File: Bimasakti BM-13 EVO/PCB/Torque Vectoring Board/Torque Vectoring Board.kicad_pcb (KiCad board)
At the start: 2 copper layers, 63.6 x 82.8 mm, 1 part

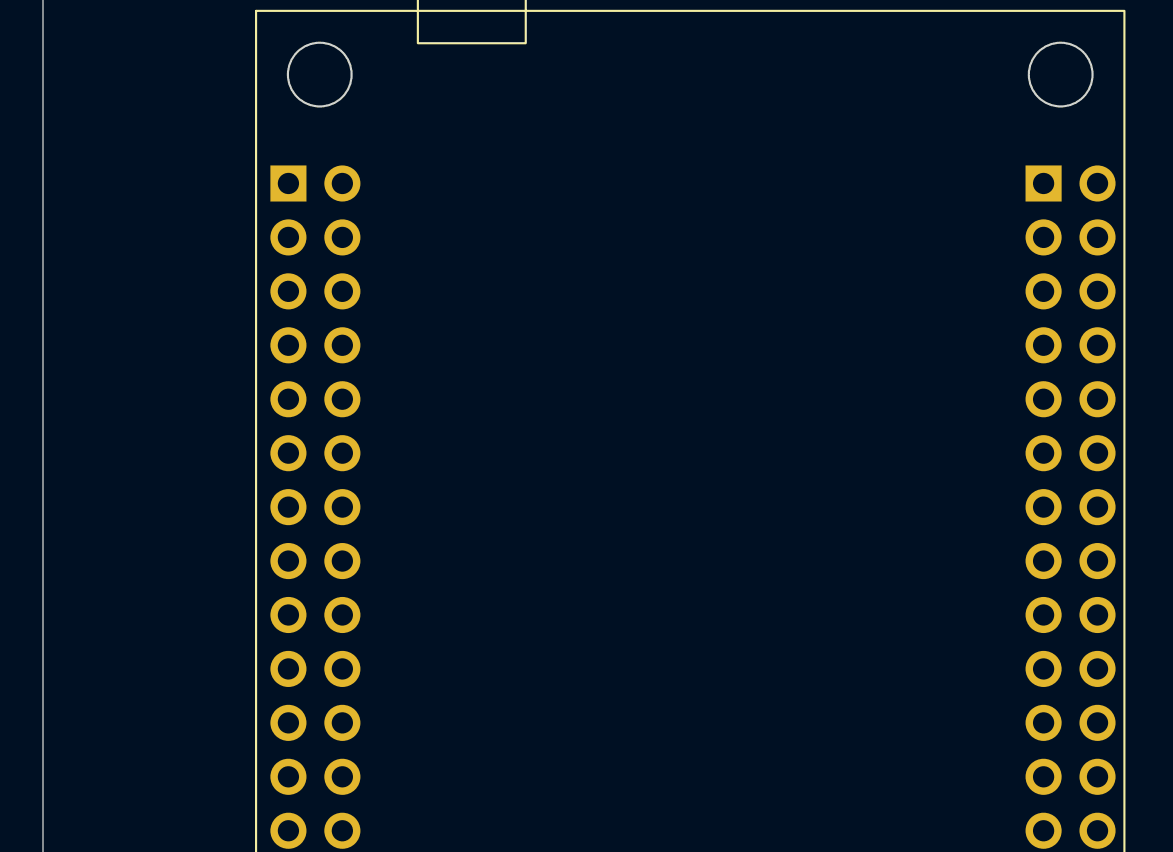
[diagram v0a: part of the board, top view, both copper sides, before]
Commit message: pdm finishing tambah logo
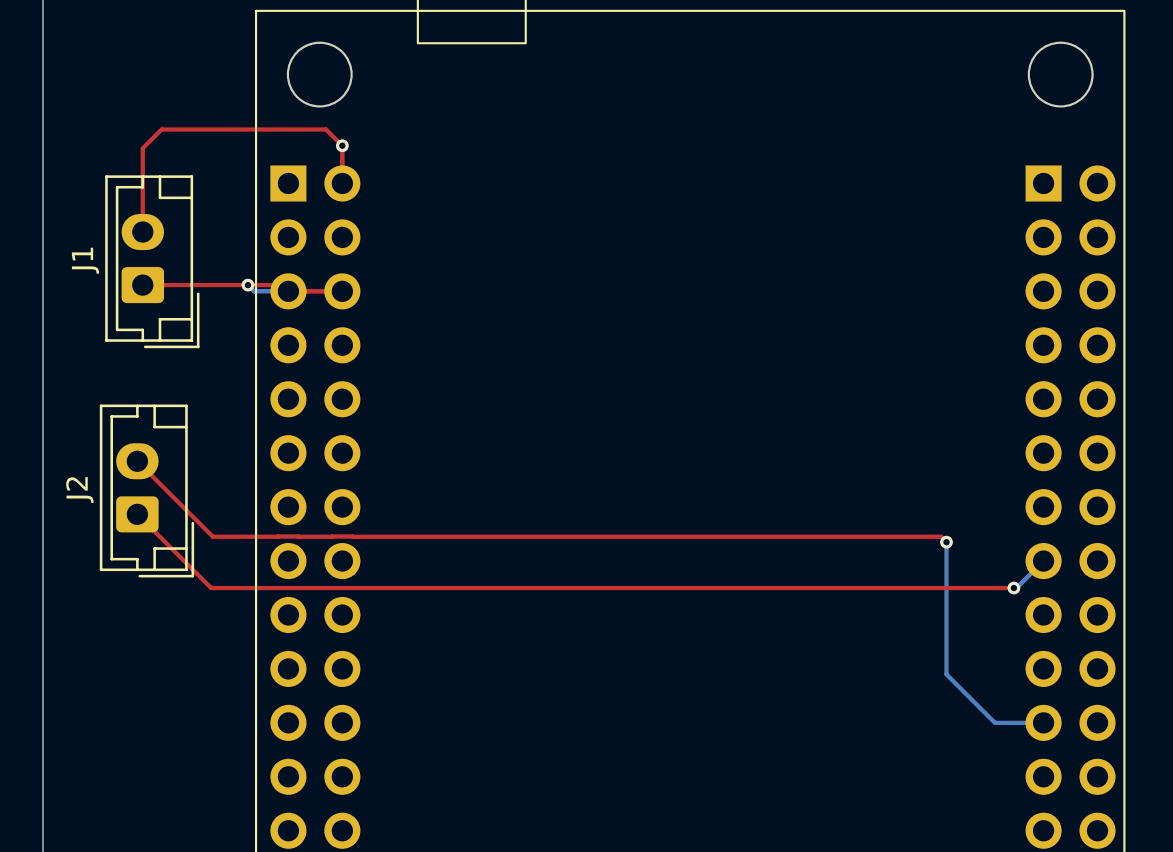
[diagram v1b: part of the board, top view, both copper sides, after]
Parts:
- added J1: Conn_01x02_Socket, Connector_JST:JST_EH_B2B-EH-A_1x02_P2.50mm_Vertical, F.Cu at (82.5, 60.3)
- added J2: Conn_01x02_Socket, Connector_JST:JST_EH_B2B-EH-A_1x02_P2.50mm_Vertical, F.Cu at (82.3, 71.1)
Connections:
- U1 pad 2: unconnected-(U1-5V-Pad2) -> Net-(J1-Pin_2)
- U1 pad 5: unconnected-(U1-GND-Pad5) -> GND
- U1 pad 59: unconnected-(U1-PE13-Pad59) -> Net-(J2-Pin_1)
- U1 pad 6: unconnected-(U1-GND-Pad6) -> GND
- U1 pad 65: unconnected-(U1-PE7-Pad65) -> Net-(J2-Pin_2)
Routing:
- net Net-(J2-Pin_2): track 0.00 -> 51.4 mm, vias 0 -> 1
- net Net-(J2-Pin_1): track 0.00 -> 44.8 mm, vias 0 -> 1
- net Net-(J1-Pin_2): track 0.00 -> 17.6 mm, vias 0 -> 1
- net GND: track 0.00 -> 14.1 mm, vias 0 -> 1

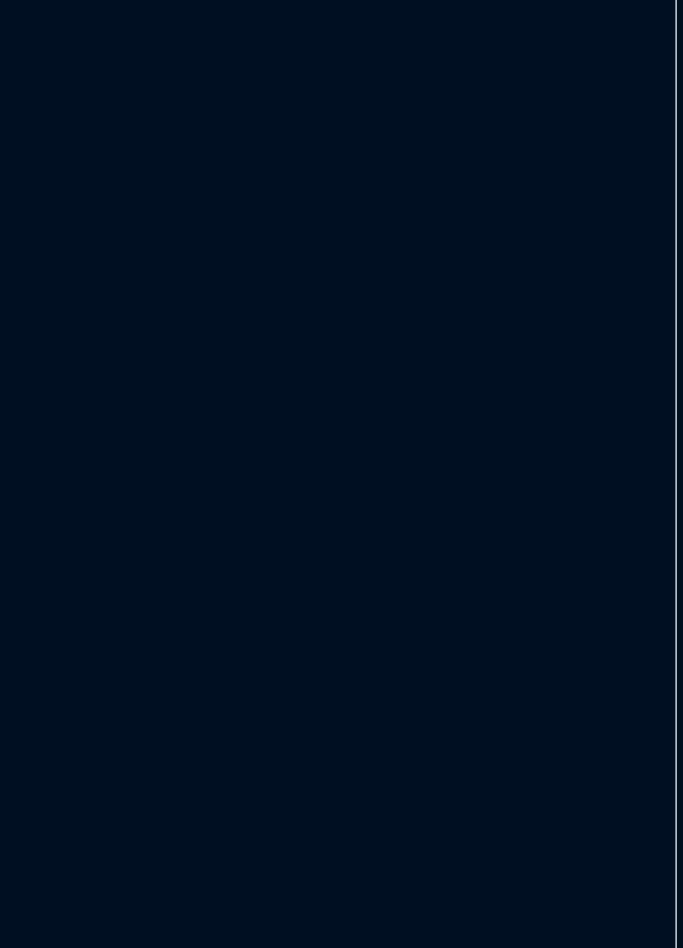
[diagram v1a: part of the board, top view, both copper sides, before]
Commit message: torque vectoring
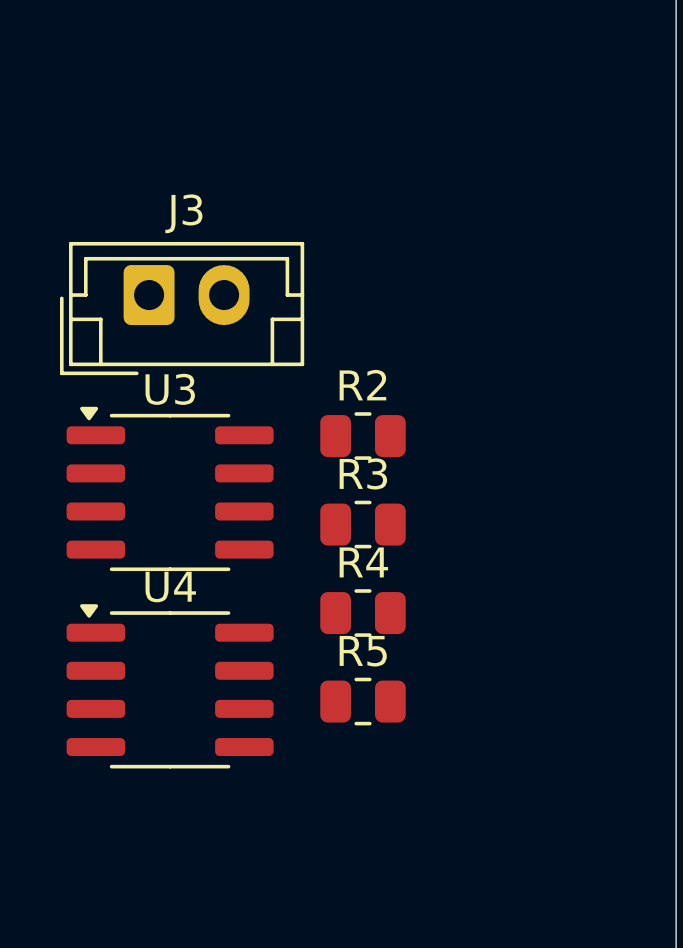
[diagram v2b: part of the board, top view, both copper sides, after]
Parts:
- added J3: Can ESC 2, Connector_JST:JST_EH_B2B-EH-A_1x02_P2.50mm_Vertical, F.Cu at (60.3, 77.3)
- added R2: R, Resistor_SMD:R_0805_2012Metric, F.Cu at (67.4, 82.0)
- added R3: R, Resistor_SMD:R_0805_2012Metric, F.Cu at (67.4, 84.9)
- added R4: R, Resistor_SMD:R_0805_2012Metric, F.Cu at (67.4, 87.9)
- added R5: R, Resistor_SMD:R_0805_2012Metric, F.Cu at (67.4, 90.8)
- added U3: SN65HVD230, Package_SO:SOIC-8_3.9x4.9mm_P1.27mm, F.Cu at (61.0, 83.8)
- added U4: SN65HVD230, Package_SO:SOIC-8_3.9x4.9mm_P1.27mm, F.Cu at (61.0, 90.4)
- J2: value Conn_01x02_Socket -> Can ESC 1
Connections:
- J2 pad 1: Net-(J2-Pin_1) -> CANH1
- J2 pad 2: Net-(J2-Pin_2) -> CANL1
- U1 pad 21: unconnected-(U1-PA11/USBM-Pad21) -> CAN1_TX
- U1 pad 24: unconnected-(U1-PA12/USB_DP-Pad24) -> CAN1_RX
- U1 pad 3: unconnected-(U1-3V3-Pad3) -> 3V3
- U1 pad 39: unconnected-(U1-PB7-Pad39) -> SDA
- U1 pad 4: unconnected-(U1-3V3-Pad4) -> 3V3
- U1 pad 40: unconnected-(U1-PB6-Pad40) -> SCL
- U1 pad 53: unconnected-(U1-PB13-Pad53) -> CAN2_RX
- U1 pad 54: unconnected-(U1-PB12-Pad54) -> CAN2_TX
- U1 pad 59: Net-(J2-Pin_1) -> unconnected-(U1-PE13-Pad59)
- U1 pad 65: Net-(J2-Pin_2) -> unconnected-(U1-PE7-Pad65)
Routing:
- net (no net): track 0.00 -> 96.2 mm, vias 0 -> 2
- net Net-(J2-Pin_2): track 51.4 -> 0.00 mm, vias 1 -> 0
- net Net-(J2-Pin_1): track 44.8 -> 0.00 mm, vias 1 -> 0

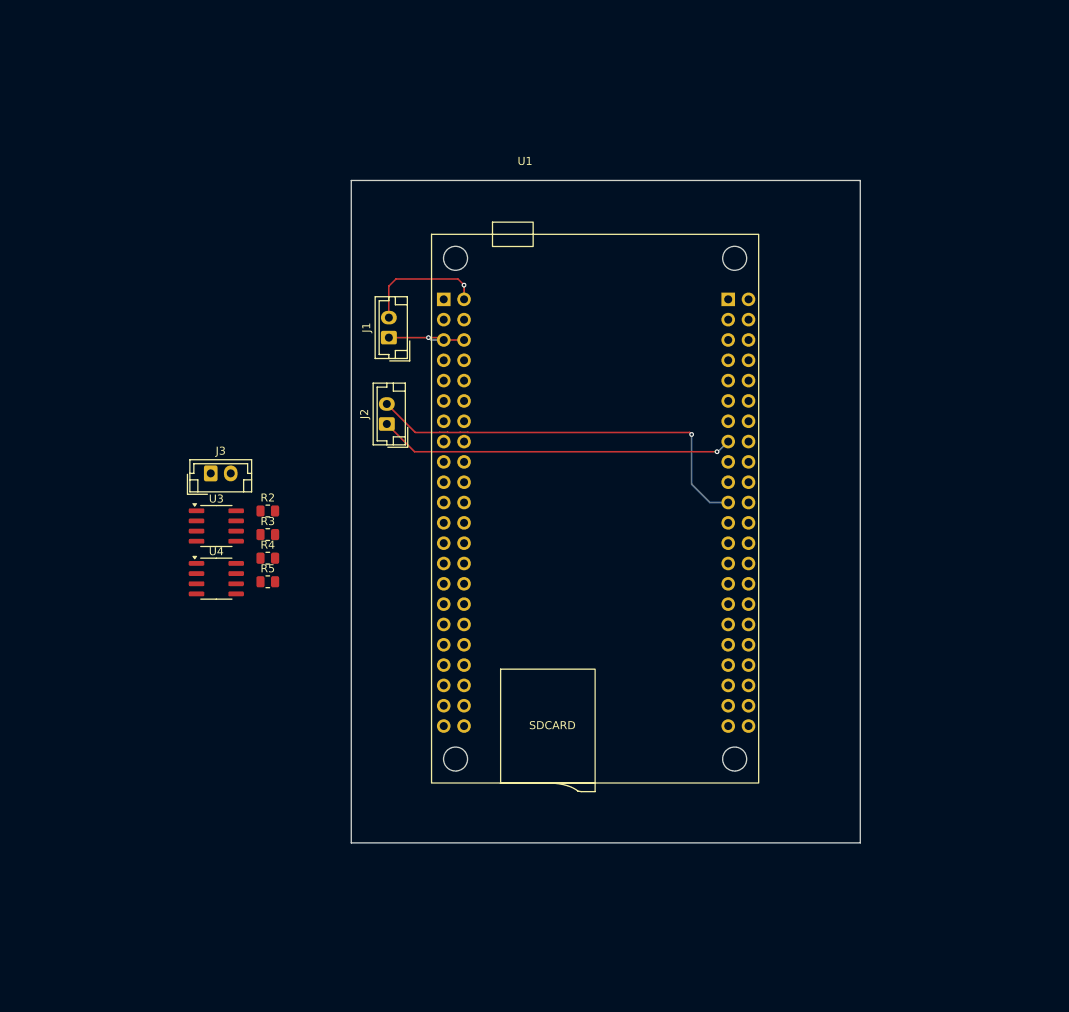
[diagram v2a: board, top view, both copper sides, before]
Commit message: tv board kurang IMU
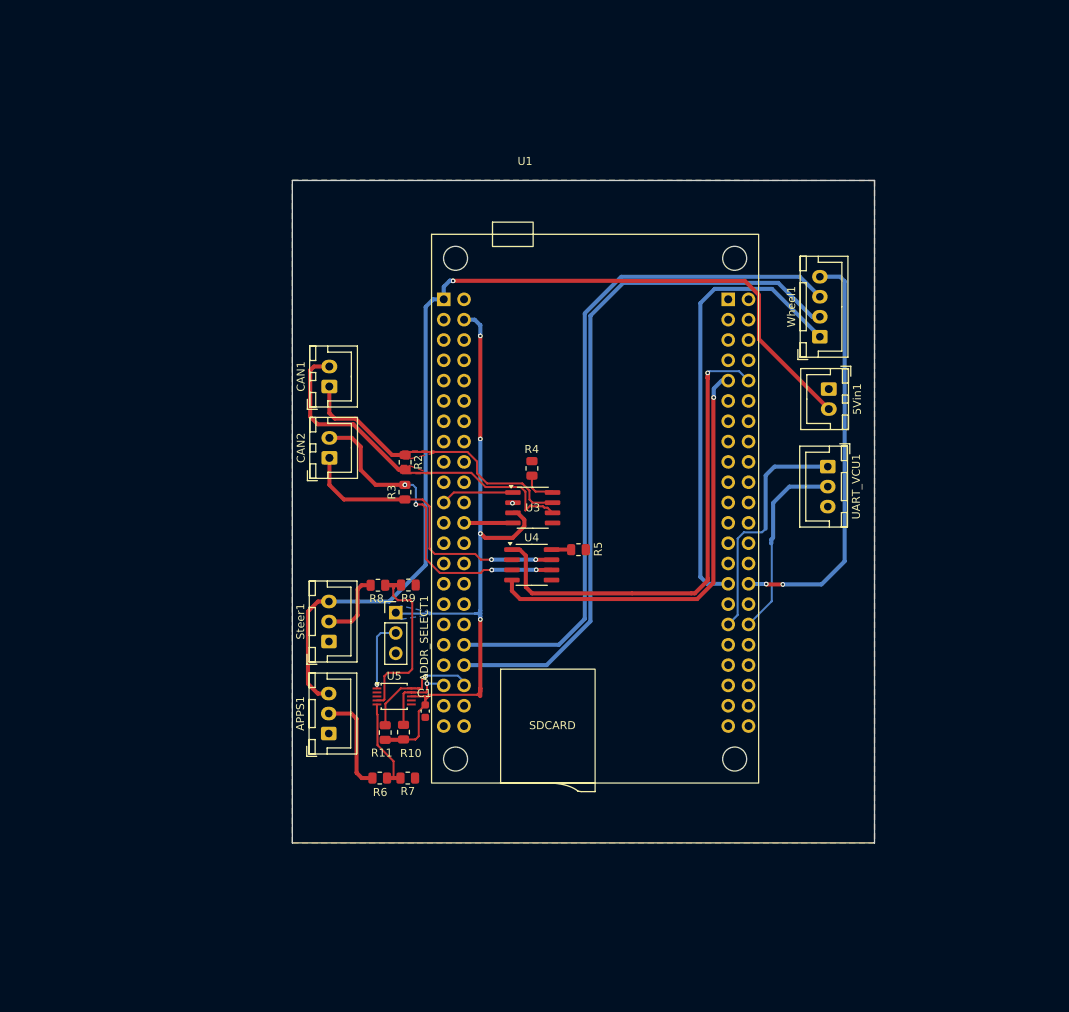
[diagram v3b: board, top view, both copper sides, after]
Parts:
- removed J1: Conn_01x02_Socket, Connector_JST:JST_EH_B2B-EH-A_1x02_P2.50mm_Vertical
- removed J2: Can ESC 1, Connector_JST:JST_EH_B2B-EH-A_1x02_P2.50mm_Vertical
- removed J3: Can ESC 2, Connector_JST:JST_EH_B2B-EH-A_1x02_P2.50mm_Vertical
- added 5Vin1: Conn_01x02, Connector_JST:JST_XH_B2B-XH-A_1x02_P2.50mm_Vertical, F.Cu at (137.5, 66.7)
- added ADDR_SELECT1: Conn_01x03, Connector_PinHeader_2.54mm:PinHeader_1x03_P2.54mm_Vertical, F.Cu at (83.4, 94.7)
- added APPS1: Conn_01x03, Connector_JST:JST_XH_B3B-XH-A_1x03_P2.50mm_Vertical, F.Cu at (75.0, 109.8)
- added C1: 0.1uF, Capacitor_SMD:C_0603_1608Metric, F.Cu at (87.1, 107.0)
- added CAN1: Conn_01x02, Connector_JST:JST_XH_B2B-XH-A_1x02_P2.50mm_Vertical, F.Cu at (75.1, 66.4)
- added CAN2: Conn_01x02, Connector_JST:JST_XH_B2B-XH-A_1x02_P2.50mm_Vertical, F.Cu at (75.1, 75.3)
- added R10: 10K, Resistor_SMD:R_0805_2012Metric, F.Cu at (84.4, 109.6)
- added R11: 10K, Resistor_SMD:R_0805_2012Metric, F.Cu at (82.1, 109.6)
- added R6: 5K, Resistor_SMD:R_0805_2012Metric, F.Cu at (81.4, 115.3)
- added R7: 3K3, Resistor_SMD:R_0805_2012Metric, F.Cu at (84.9, 115.3)
- added R8: 5K, Resistor_SMD:R_0805_2012Metric, F.Cu at (81.2, 91.2)
- added R9: 3K3, Resistor_SMD:R_0805_2012Metric, F.Cu at (85.0, 91.2)
- added Steer1: Conn_01x03, Connector_JST:JST_XH_B3B-XH-A_1x03_P2.50mm_Vertical, F.Cu at (75.1, 98.3)
- added U5: ADS1115IDGS, Package_SO:TSSOP-10_3x3mm_P0.5mm, F.Cu at (83.2, 105.1)
- added UART_VCU1: Conn_01x03, Connector_JST:JST_XH_B3B-XH-A_1x03_P2.50mm_Vertical, F.Cu at (137.4, 76.4)
- added Wheel1: Conn_01x04, Connector_JST:JST_XH_B4B-XH-A_1x04_P2.50mm_Vertical, F.Cu at (136.4, 60.2)
- R2, R3: value R -> 120
- R4, R5: value R -> 1K
- moved U3 39.6 mm to (100.5, 81.5)
- moved U4 39.5 mm to (100.4, 88.7)
- moved R5 39.0 mm to (106.3, 86.8), turned to 180 degrees
- moved R4 34.9 mm to (100.4, 76.6), turned to -90 degrees
- moved R2 18.2 mm to (84.6, 75.9), turned to -90 degrees
- moved R3 17.9 mm to (84.6, 79.6), turned to 90 degrees
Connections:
- U1 pad 1: unconnected-(U1-5V-Pad1) -> 5V
- U1 pad 2: Net-(J1-Pin_2) -> unconnected-(U1-5V-Pad2)
- U1 pad 36: unconnected-(U1-PD7-Pad36) -> MOSI
- U1 pad 38: unconnected-(U1-PB4-Pad38) -> MISO
- U1 pad 72: unconnected-(U1-PA6-Pad72) -> GPOS
- U1 pad 73: unconnected-(U1-PA5-Pad73) -> SCK
- U1 pad 74: unconnected-(U1-PA4-Pad74) -> SS
- U1 pad 77: unconnected-(U1-PA1-Pad77) -> TX1
- U1 pad 78: unconnected-(U1-PA0-Pad78) -> RX1
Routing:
- net 5V: track 0.00 -> 124.1 mm, vias 0 -> 1
- net (no net): track 96.2 -> 0.00 mm, vias 2 -> 0
- net 3V3: track 0.00 -> 90.6 mm, vias 0 -> 4
- net MISO: track 0.00 -> 88.4 mm
- net MOSI: track 0.00 -> 86.9 mm
- net CAN2_TX: track 0.00 -> 61.7 mm, vias 0 -> 1
- net SCK: track 0.00 -> 56.2 mm
- net CAN2_RX: track 0.00 -> 54.4 mm, vias 0 -> 1
- net SS: track 0.00 -> 51.6 mm, vias 0 -> 2
- net CANL1: track 0.00 -> 45.6 mm
- net CANL2: track 0.00 -> 41.6 mm, vias 0 -> 4
- net CANH2: track 0.00 -> 38.1 mm, vias 0 -> 2
- net CANH1: track 0.00 -> 37.7 mm
- net TX1: track 0.00 -> 30.1 mm
- net RX1: track 0.00 -> 24.3 mm
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- added copper zone on B.Cu, net 3V3
- added copper zone on F.Cu, net CANH1
- added copper zone on F.Cu, net CANL1
- added copper zone on B.Cu, net GND
- added copper zone on F.Cu, net GND
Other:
- board size 63.6 x 82.8 mm -> 72.8 x 82.8 mm

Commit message: cicil assembly
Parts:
- added H1: MountingHole_Pad, MountingHole:MountingHole_3.2mm_M3_ISO7380_Pad_TopBottom, F.Cu at (146.5, 34.2)
- added H2: MountingHole_Pad, MountingHole:MountingHole_3.2mm_M3_ISO7380_Pad_TopBottom, F.Cu at (48.8, 34.0)
- added H3: MountingHole_Pad, MountingHole:MountingHole_3.2mm_M3_ISO7380_Pad_TopBottom, F.Cu at (142.2, 131.6)
- added H4: MountingHole_Pad, MountingHole:MountingHole_3.2mm_M3_ISO7380_Pad_TopBottom, F.Cu at (48.3, 132.1)
- added R12: 10K, Resistor_SMD:R_0805_2012Metric, F.Cu at (99.3, 42.5)
- added R13: 10K, Resistor_SMD:R_0805_2012Metric, F.Cu at (97.0, 42.5)
- added U2: ~, 0_bno055:0_BNO055, F.Cu at (94.9, 25.9)
- moved CAN1 77.9 mm to (117.8, 131.6), turned to 180 degrees
- moved ADDR_SELECT1 77.1 mm to (131.3, 34.3), turned to 90 degrees
- moved 5Vin1 75.6 mm to (98.6, 131.6), turned to 180 degrees
- moved C1 75.3 mm to (63.4, 35.5), turned to 180 degrees
- moved UART_VCU1 73.1 mm to (89.4, 131.6), turned to 180 degrees
- moved R6 71.8 mm to (66.8, 45.1), turned to 90 degrees
- moved Wheel1 71.5 mm to (132.0, 131.6), turned to 180 degrees
- moved R7 71.4 mm to (72.1, 45.1), turned to -90 degrees
- moved R10 69.6 mm to (80.4, 40.1), turned to 0 degrees
- moved R11 67.5 mm to (80.4, 42.2), turned to 0 degrees
- moved CAN2 65.1 mm to (107.9, 131.6), turned to 180 degrees
- moved U4 61.6 mm to (140.0, 41.4), turned to 90 degrees
- moved U5 59.8 mm to (79.2, 45.5)
- moved R2 58.4 mm to (126.7, 35.5)
- moved R3 58.4 mm to (126.7, 39.2)
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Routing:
- net 5V: track 124.1 -> 0.00 mm, vias 1 -> 0
- net MISO: track 88.4 -> 0.00 mm
- net MOSI: track 86.9 -> 0.00 mm
- net 3V3: track 90.6 -> 6.77 mm, vias 4 -> 0
- net SDA: track 10.2 -> 73.7 mm, vias 1 -> 0
- net CAN2_TX: track 61.7 -> 0.00 mm, vias 1 -> 0
- net SCL: track 16.5 -> 76.7 mm, vias 1 -> 0
- net SCK: track 56.2 -> 0.00 mm
- net CAN2_RX: track 54.4 -> 0.00 mm, vias 1 -> 0
- net SS: track 51.6 -> 0.00 mm, vias 2 -> 0
- net CANL1: track 45.6 -> 0.00 mm
- net CANL2: track 41.6 -> 0.00 mm, vias 4 -> 0
- net CANH2: track 38.1 -> 0.00 mm, vias 2 -> 0
- net CANH1: track 37.7 -> 0.00 mm
- net TX1: track 30.1 -> 0.00 mm
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- removed copper zone on B.Cu, net 3V3
- removed copper zone on F.Cu, net CANH1
- removed copper zone on F.Cu, net CANL1
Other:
- board size 72.8 x 82.8 mm -> 108 x 110 mm
